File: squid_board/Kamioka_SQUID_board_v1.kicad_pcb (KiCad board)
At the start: 2 copper layers, 72.1 x 111.2 mm, 18 parts, among them J1 Conn_01x25, J6 Conn_01x51

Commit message: add SQUID board changes
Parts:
- moved H7 73.5 mm to (168.0, 134.0)
- moved H6 54.8 mm to (104.0, 134.0)
- moved SQ4 20.2 mm to (160.0, 41.3)
- moved H4 20.2 mm to (160.0, 33.2)
- moved H8 20.1 mm to (168.0, 104.0)
- moved SQ3 19.0 mm to (144.0, 41.3)
- moved H3 19.0 mm to (144.0, 33.2)
- moved J1 18.5 mm to (135.4, 131.7)
- moved J6 18.5 mm to (114.0, 122.7)
- moved R2 18.5 mm to (128.0, 112.5)
- moved R3 18.5 mm to (133.0, 112.5)
- moved R1 18.5 mm to (117.8, 112.4)
- moved R4 18.5 mm to (138.0, 112.5)
- moved H5 18.4 mm to (104.0, 104.0)
- moved SQ2 18.0 mm to (127.7, 41.3)
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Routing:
- net /Ch3_3: track 118.1 -> 112.9 mm
- net /h+sq_1: track 101.7 -> 105.2 mm
- net /Ch2_3: track 107.9 -> 104.6 mm
- net /I+sq_4: track 111.0 -> 114.0 mm
- net /fb+sq_4: track 87.0 -> 89.9 mm
- net /I-sq_1: track 84.7 -> 87.5 mm
- net /I+_sq1: track 86.8 -> 89.5 mm
- net /h+sq_4: track 90.8 -> 93.4 mm
- net /fb+sq_1: track 108.0 -> 110.6 mm
- net /I-sq_4: track 109.7 -> 112.3 mm
- net /fb-sq_1: track 105.3 -> 107.7 mm
- net /b+TES1: track 84.6 -> 86.9 mm
- net /b+TES3: track 88.9 -> 86.7 mm
- net /fb-sq_4: track 86.6 -> 88.6 mm
- net /h+sq_3: track 79.7 -> 77.9 mm
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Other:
- board size 72.1 x 111.2 mm -> 72 x 110 mm

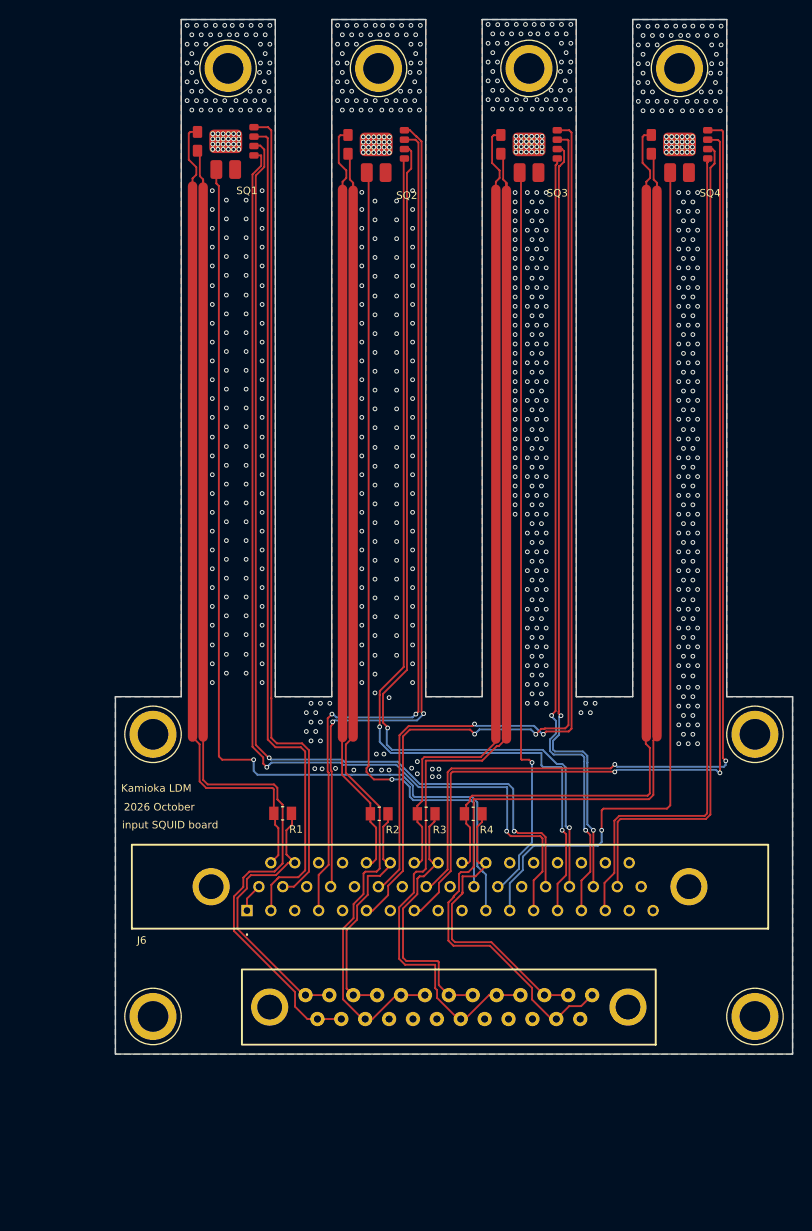
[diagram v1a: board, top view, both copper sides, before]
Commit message: Clean up ground paths and add new stepfile
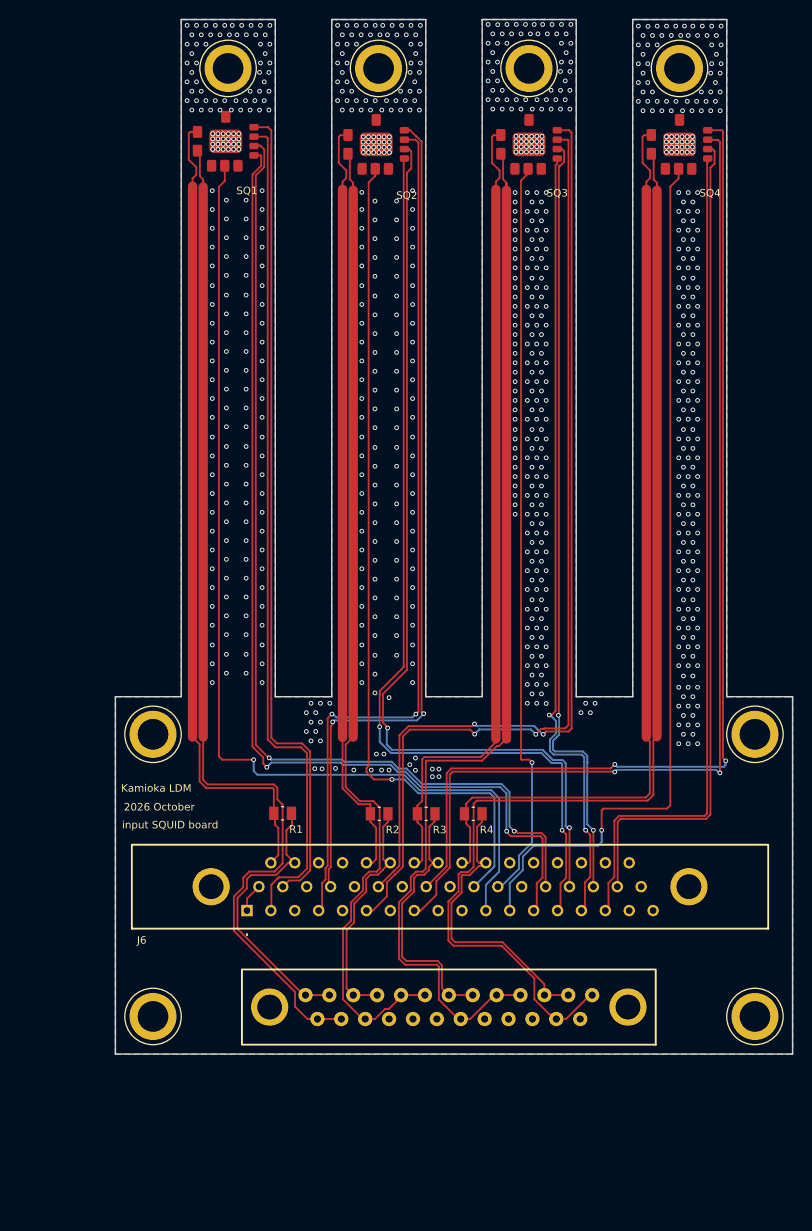
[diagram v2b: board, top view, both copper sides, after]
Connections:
- SQ1 pad 3: /h+sq_1 -> GND
- SQ1 pad 4: GND -> /h+sq_1
- SQ1 pad 5: /fb+sq_1 -> GND
- SQ1 pad 6: /fb-sq_1 -> /fb+sq_1
- SQ1 pad 7: /I+_sq1 -> /fb-sq_1
- SQ1 pad 8: /I-sq_1 -> /I+_sq1
- SQ1 pad 9: GND -> /I-sq_1
- SQ2 pad 3: /h+sq_2 -> GND
- SQ2 pad 4: GND -> /h+sq_2
- SQ2 pad 5: /fb+sq_2 -> GND
- SQ2 pad 6: /fb-sq_2 -> /fb+sq_2
- SQ2 pad 7: /I+sq_2 -> /fb-sq_2
- SQ2 pad 8: /I-sq_2 -> /I+sq_2
- SQ2 pad 9: GND -> /I-sq_2
- SQ3 pad 3: /h+sq_3 -> GND
- SQ3 pad 4: GND -> /h+sq_3
- SQ3 pad 5: /fb+sq_3 -> GND
- SQ3 pad 6: /fb-sq_3 -> /fb+sq_3
- SQ3 pad 7: /I+sq_3 -> /fb-sq_3
- SQ3 pad 8: /I-sq_3 -> /I+sq_3
- SQ3 pad 9: GND -> /I-sq_3
- SQ4 pad 3: /h+sq_4 -> GND
- SQ4 pad 4: GND -> /h+sq_4
- SQ4 pad 5: /fb+sq_4 -> GND
- SQ4 pad 6: /fb-sq_4 -> /fb+sq_4
- SQ4 pad 7: /I+sq_4 -> /fb-sq_4
- SQ4 pad 8: /I-sq_4 -> /I+sq_4
- SQ4 pad 9: GND -> /I-sq_4
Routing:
- net /h+sq_2: track 85.8 -> 89.6 mm
- net /h+sq_1: track 105.2 -> 108.0 mm
- net /Ch4_3: track 125.0 -> 126.3 mm
- net /Ch2_3: track 104.6 -> 105.6 mm
- net /h+sq_3: track 77.9 -> 78.8 mm
- net /Ch4_1: track 31.1 -> 32.0 mm
- net /h+sq_4: track 93.4 -> 94.3 mm
- net /b+TES2: track 81.0 -> 81.7 mm
- net /fb+sq_2: track 100.0 -> 99.5 mm
- net /Ch3_1: track 28.5 -> 29.0 mm

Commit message: latest update
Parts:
- added H10: MountingHole_Pad, MountingHole:MountingHole_2.2mm_M2_DIN965_Pad_TopBottom, F.Cu at (112.7, 70.0)
- added H11: MountingHole_Pad, MountingHole:MountingHole_2.2mm_M2_DIN965_Pad_TopBottom, F.Cu at (112.7, 90.0)
- added H12: MountingHole_Pad, MountingHole:MountingHole_2.2mm_M2_DIN965_Pad_TopBottom, F.Cu at (128.7, 50.0)
- added H13: MountingHole_Pad, MountingHole:MountingHole_2.2mm_M2_DIN965_Pad_TopBottom, F.Cu at (128.7, 70.0)
- added H14: MountingHole_Pad, MountingHole:MountingHole_2.2mm_M2_DIN965_Pad_TopBottom, F.Cu at (128.7, 90.0)
- added H15: MountingHole_Pad, MountingHole:MountingHole_2.2mm_M2_DIN965_Pad_TopBottom, F.Cu at (144.7, 50.0)
- added H16: MountingHole_Pad, MountingHole:MountingHole_2.2mm_M2_DIN965_Pad_TopBottom, F.Cu at (144.7, 70.0)
- added H17: MountingHole_Pad, MountingHole:MountingHole_2.2mm_M2_DIN965_Pad_TopBottom, F.Cu at (144.7, 90.0)
- added H18: MountingHole_Pad, MountingHole:MountingHole_2.2mm_M2_DIN965_Pad_TopBottom, F.Cu at (160.7, 50.0)
- added H19: MountingHole_Pad, MountingHole:MountingHole_2.2mm_M2_DIN965_Pad_TopBottom, F.Cu at (160.7, 70.0)
- added H20: MountingHole_Pad, MountingHole:MountingHole_2.2mm_M2_DIN965_Pad_TopBottom, F.Cu at (160.7, 90.0)
- added H9: MountingHole_Pad, MountingHole:MountingHole_2.2mm_M2_DIN965_Pad_TopBottom, F.Cu at (112.7, 50.0)
- turned H1 to 90 degrees
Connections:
- J1 pad MH2: (no net) -> GND
- J6 pad MH1: (no net) -> GND
- J6 pad MH2: (no net) -> GND
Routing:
- net /Ch1_3: track 111.2 -> 115.6 mm
- net /Ch1_1: track 29.6 -> 33.2 mm
- net /Ch2_3: track 105.6 -> 103.9 mm
- net /Ch4_1: track 32.0 -> 33.7 mm
- net /fb+sq_1: track 110.2 -> 109.0 mm
- net /h+sq_4: track 94.3 -> 93.3 mm
- net /h+sq_2: track 89.6 -> 90.5 mm
- net /I-sq_2: track 90.8 -> 91.6 mm
- net /fb+sq_2: track 99.5 -> 100.2 mm
- net /Ch4_3: track 126.3 -> 125.5 mm
- net /fb-sq_1: track 107.2 -> 106.5 mm
- net /h+sq_1: track 108.0 -> 107.3 mm
- net /Ch3_1: track 29.0 -> 28.3 mm
- net /I-sq_1: track 87.6 -> 87.0 mm
- net /I+_sq1: track 89.7 -> 89.1 mm
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
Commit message: add udpated pcb
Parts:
- added C1: C, Capacitor_SMD:C_0805_2012Metric, F.Cu at (108.8, 46.6)
- added C2: C, Capacitor_SMD:C_0805_2012Metric, F.Cu at (124.8, 46.3)
- added C3: C, Capacitor_SMD:C_0805_2012Metric, F.Cu at (140.9, 46.3)
- added C4: C, Capacitor_SMD:C_0805_2012Metric, F.Cu at (156.9, 46.3)
- added C5: C, Capacitor_SMD:C_0805_2012Metric, F.Cu at (115.3, 45.9)
- added C6: C, Capacitor_SMD:C_0805_2012Metric, F.Cu at (131.3, 45.9)
- added C7: C, Capacitor_SMD:C_0805_2012Metric, F.Cu at (147.3, 45.9)
- added C8: C, Capacitor_SMD:C_0805_2012Metric, F.Cu at (163.3, 45.9)
- added R10: R_US, Capacitor_SMD:C_0805_2012Metric, F.Cu at (131.3, 47.9)
- added R11: R_US, Capacitor_SMD:C_0805_2012Metric, F.Cu at (147.3, 47.9)
- added R12: R_US, Capacitor_SMD:C_0805_2012Metric, F.Cu at (163.3, 47.9)
- added R13: R_US, Capacitor_SMD:C_0805_2012Metric, F.Cu at (114.0, 50.1)
- added R14: R_US, Capacitor_SMD:C_0805_2012Metric, F.Cu at (129.9, 50.1)
- added R15: R_US, Capacitor_SMD:C_0805_2012Metric, F.Cu at (145.9, 50.1)
- added R16: R_US, Capacitor_SMD:C_0805_2012Metric, F.Cu at (161.9, 50.1)
- added R5: R_US, Resistor_SMD:R_0805_2012Metric, F.Cu at (108.7, 50.1)
- added R6: R_US, Resistor_SMD:R_0805_2012Metric, F.Cu at (124.7, 49.8)
- added R7: R_US, Resistor_SMD:R_0805_2012Metric, F.Cu at (140.8, 49.8)
- added R8: R_US, Resistor_SMD:R_0805_2012Metric, F.Cu at (156.8, 49.8)
- added R9: R_US, Capacitor_SMD:C_0805_2012Metric, F.Cu at (115.3, 47.9)
- moved H12 5.00 mm to (128.7, 55.0)
- moved H15 5.00 mm to (144.7, 55.0)
- moved H18 5.00 mm to (160.7, 55.0)
- moved H9 5.00 mm to (112.7, 55.0)
- moved SQ2 0.32 mm to (127.7, 41.0)
- moved SQ3 0.32 mm to (144.0, 41.0)
- moved SQ4 0.32 mm to (160.0, 41.0)
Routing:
- net /Ch2_3: track 103.9 -> 109.9 mm
- net /Ch3_3: track 112.8 -> 116.9 mm
- net /Ch4_3: track 125.5 -> 129.3 mm
- net /Ch1_3: track 115.6 -> 118.7 mm
- net /I+sq_2: track 93.1 -> 95.8 mm
- net /fb-sq_3: track 83.1 -> 85.7 mm
- net /I+sq_3: track 103.2 -> 105.6 mm
- net /I+sq_4: track 113.8 -> 116.2 mm
- net /I+_sq1: track 89.1 -> 91.6 mm
- net /fb-sq_4: track 88.5 -> 90.9 mm
- net /fb+sq_3: track 85.0 -> 87.4 mm
- net /fb-sq_1: track 106.5 -> 108.8 mm
- net /fb+sq_1: track 109.0 -> 111.2 mm
- net /fb-sq_2: track 98.8 -> 100.7 mm
- net /fb+sq_4: track 90.1 -> 91.8 mm
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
